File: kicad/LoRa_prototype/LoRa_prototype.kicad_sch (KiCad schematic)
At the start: 6 parts, among them J1 Conn_ST_STDC14, J2 U.FL, U3 AS179-92LF

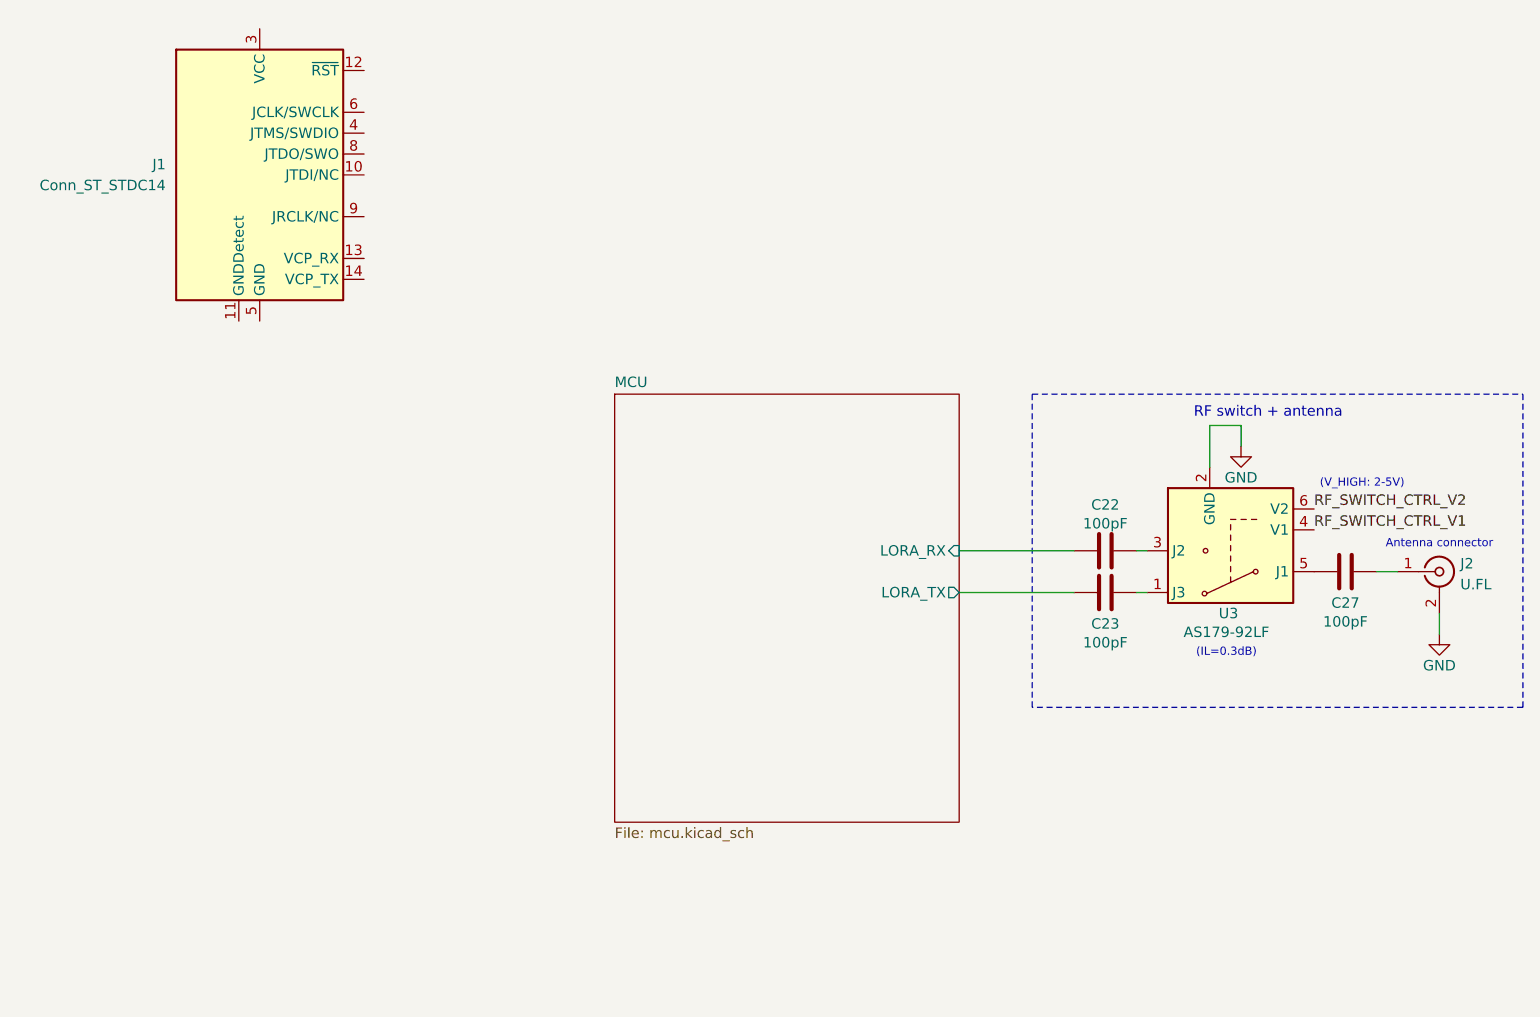
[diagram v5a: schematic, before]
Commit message: Schematic for programming interface done
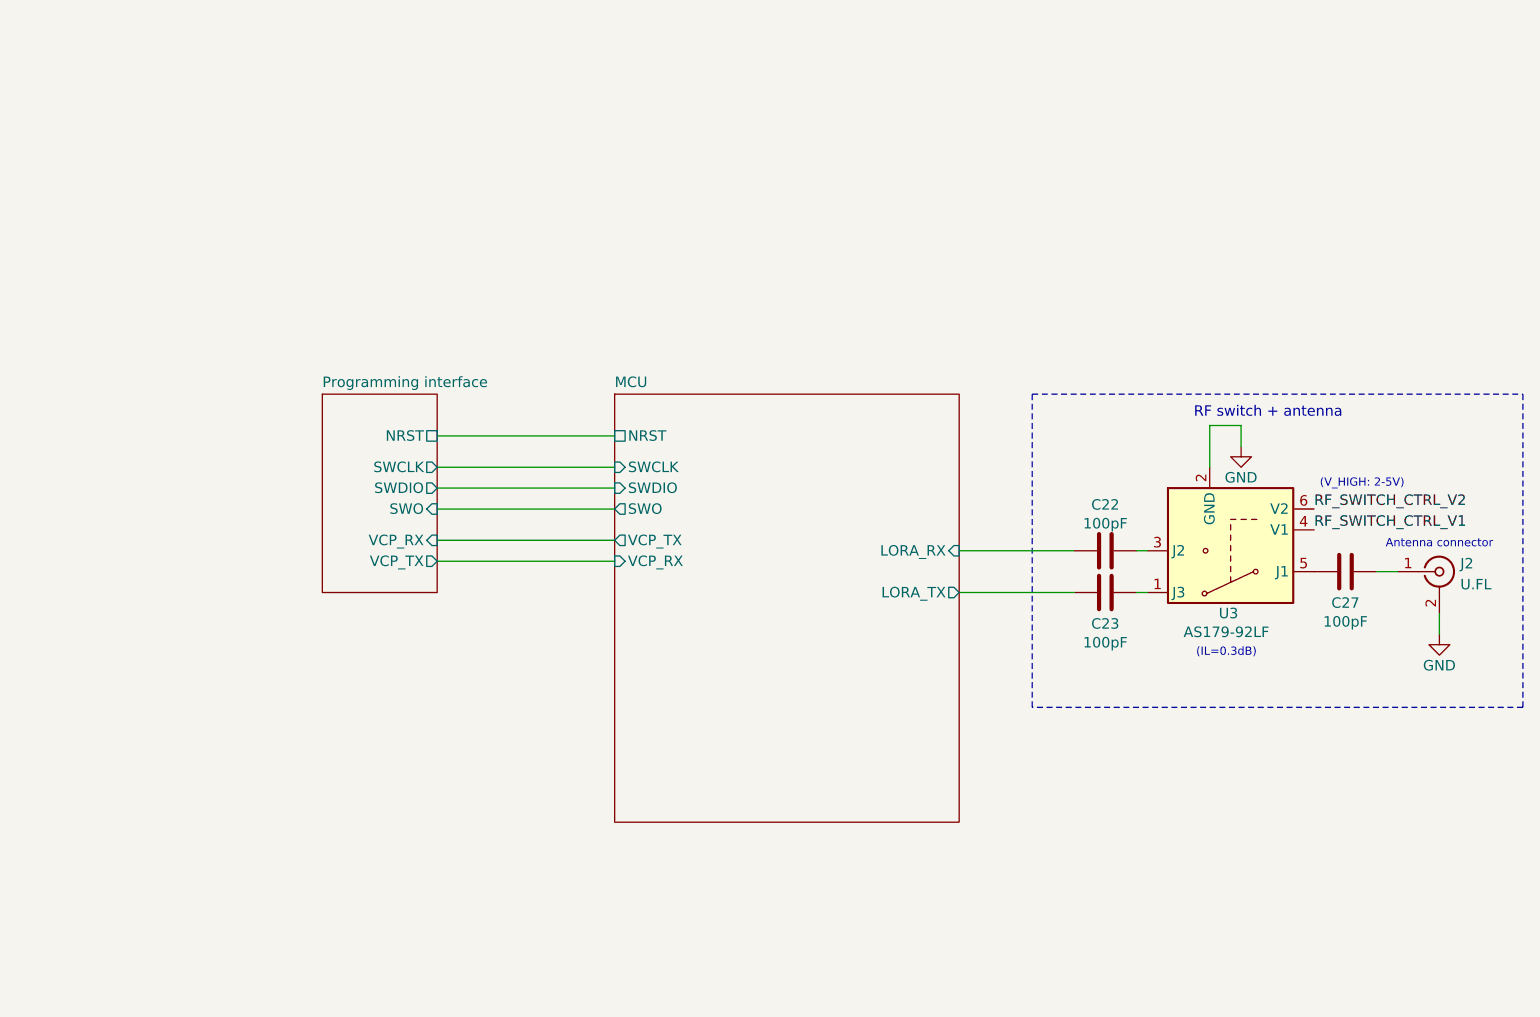
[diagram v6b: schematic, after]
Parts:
- removed J1: Conn_ST_STDC14, Connector_PinHeader_1.27mm:PinHeader_2x07_P1.27mm_Vertical, symbol Connector:Conn_ST_STDC14
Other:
- added sheet Programming interface (programming_interface.kicad_sch)
- sheet MCU ports: added NRST, SWCLK, SWDIO, SWO, VCP_RX, VCP_TX; removed none
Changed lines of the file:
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@@
+	(wire
+		(pts
+			(xy 74.93 96.52) (xy 96.52 96.52)
+		)
+		(stroke
+			(width 0)
+			(type default)
+		)
+	)
 	(wire
 		(pts
@@
 	(wire
 		(pts
+			(xy 74.93 93.98) (xy 96.52 93.98)
+		)
+		(stroke
+			(width 0)
+			(type default)
+		)
+	)
+	(wire
+		(pts
+			(xy 74.93 81.28) (xy 96.52 81.28)
+		)
+		(stroke
+			(width 0)
+			(type default)
+		)
+	)
+	(wire
+		(pts
+			(xy 74.93 90.17) (xy 96.52 90.17)
+		)
+		(stroke
+			(width 0)
+			(type default)
+		)
+	)
+	(wire
+		(pts
 			(xy 172.72 82.55) (xy 172.72 80.01)
 		)
@@
 	(wire
 		(pts
+			(xy 74.93 85.09) (xy 96.52 85.09)
+		)
+		(stroke
+			(width 0)
+			(type default)
+		)
+	)
+	(wire
+		(pts
 			(xy 138.43 100.33) (xy 152.4 100.33)
 		)
@@
 		(pts
 			(xy 138.43 95.25) (xy 152.4 95.25)
+		)
+		(stroke
+			(width 0)
+			(type default)
+		)
+	)
+	(wire
+		(pts
+			(xy 74.93 87.63) (xy 96.52 87.63)
 		)
 		(stroke
@@
 	)
 	(symbol
-		(lib_id "Connector:Conn_ST_STDC14")
-		(at 53.34 49.53 0)
-		(unit 1)
-		(exclude_from_sim no)
-		(in_bom yes)
-		(on_board yes)
-		(dnp no)
-		(fields_autoplaced yes)
-		(property "Reference" "J1"
-			(at 41.91 48.2599 0)
-			(effects
-				(font
-					(size 1.27 1.27)
-				)
-				(justify right)
-			)
-		)
-		(property "Value" "Conn_ST_STDC14"
-			(at 41.91 50.7999 0)
-			(effects
-				(font
-					(size 1.27 1.27)
-				)
-				(justify right)
-			)
-		)
-		(property "Footprint" "Connector_PinHeader_1.27mm:PinHeader_2x07_P1.27mm_Vertical"
-			(at 53.34 49.53 0)
-			(effects
-				(font
-					(size 1.27 1.27)
-				)
-				(hide yes)
-			)
-		)
-		(property "Datasheet" "https://www.st.com/content/ccc/resource/technical/document/user_manual/group1/99/49/91/b6/b2/3a/46/e5/DM00526767/files/DM00526767.pdf/jcr:content/translations/en.DM00526767.pdf"
-			(at 44.45 81.28 90)
-			(effects
-				(font
-					(size 1.27 1.27)
-				)
-				(hide yes)
-			)
-		)
-		(property "Description" "ST Debug Connector, standard ARM Cortex-M SWD and JTAG interface plus UART"
-			(at 53.34 49.53 0)
-			(effects
-				(font
-					(size 1.27 1.27)
-				)
-				(hide yes)
-			)
-		)
-		(pin "1"
-		)
-		(pin "12"
-		)
-		(pin "5"
-		)
-		(pin "6"
-		)
-		(pin "11"
-		)
-		(pin "13"
-		)
-		(pin "10"
-		)
-		(pin "4"
-		)
-		(pin "9"
-		)
-		(pin "8"
-		)
-		(pin "14"
-		)
-		(pin "2"
-		)
-		(pin "7"
-		)
-		(pin "3"
-		)
-		(instances
-			(project ""
-				(path "/9fad4700-f514-47ad-821a-b4076ecc08de"
-					(reference "J1")
-					(unit 1)
-				)
-			)
-		)
-	)
-	(symbol
 		(lib_id "Device:C")
 		(at 156.21 100.33 90)
@@
 	)
 	(sheet
+		(at 60.96 76.2)
+		(size 13.97 24.13)
+		(exclude_from_sim no)
+		(in_bom yes)
+		(on_board yes)
+		(dnp no)
+		(fields_autoplaced yes)
+		(stroke
+			(width 0.1524)
+			(type solid)
+		)
+		(fill
+			(color 0 0 0 0.0000)
+		)
+		(property "Sheetname" "Programming interface"
+			(at 60.96 75.4884 0)
+			(effects
+				(font
+					(size 1.27 1.27)
+				)
+				(justify left bottom)
+			)
+		)
+		(property "Sheetfile" "programming_interface.kicad_sch"
+			(at 60.96 100.9146 0)
+			(effects
+				(font
+					(size 1.27 1.27)
+				)
+				(justify left top)
+				(hide yes)
+			)
+		)
+		(pin "VCP_RX" input
+			(at 74.93 93.98 0)
+			(effects
+				(font
+					(size 1.27 1.27)
+				)
+				(justify right)
+			)
+		)
+		(pin "SWO" input
+			(at 74.93 90.17 0)
+			(effects
+				(font
+					(size 1.27 1.27)
+				)
+				(justify right)
+			)
+		)
+		(pin "VCP_TX" output
+			(at 74.93 96.52 0)
+			(effects
+				(font
+					(size 1.27 1.27)
+				)
+				(justify right)
+			)
+		)
+		(pin "SWDIO" output
+			(at 74.93 87.63 0)
+			(effects
+				(font
+					(size 1.27 1.27)
+				)
+				(justify right)
+			)
+		)
+		(pin "SWCLK" output
+			(at 74.93 85.09 0)
+			(effects
+				(font
+					(size 1.27 1.27)
+				)
+				(justify right)
+			)
+		)
+		(pin "NRST" passive
+			(at 74.93 81.28 0)
+			(effects
+				(font
+					(size 1.27 1.27)
+				)
+				(justify right)
+			)
+		)
+		(instances
+			(project "LoRa_prototype"
+				(path "/9fad4700-f514-47ad-821a-b4076ecc08de"
+					(page "3")
+				)
+			)
+		)
+	)
+	(sheet
 		(at 96.52 76.2)
 		(size 41.91 52.07)
@@
 				)
 				(justify left top)
+				(hide yes)
 			)
 		)
@@
 			)
 		)
+		(pin "NRST" passive
+			(at 96.52 81.28 180)
+			(effects
+				(font
+					(size 1.27 1.27)
+				)
+				(justify left)
+			)
+		)
+		(pin "SWDIO" input
+			(at 96.52 87.63 180)
+			(effects
+				(font
+					(size 1.27 1.27)
+				)
+				(justify left)
+			)
+		)
+		(pin "SWCLK" input
+			(at 96.52 85.09 180)
+			(effects
+				(font
+					(size 1.27 1.27)
+				)
+				(justify left)
+			)
+		)
+		(pin "SWO" output
+			(at 96.52 90.17 180)
+			(effects
+				(font
+					(size 1.27 1.27)
+				)
+				(justify left)
+			)
+		)
+		(pin "VCP_TX" output
+			(at 96.52 93.98 180)
+			(effects
+				(font
+					(size 1.27 1.27)
+				)
+				(justify left)
+			)
+		)
+		(pin "VCP_RX" input
+			(at 96.52 96.52 180)
+			(effects
+				(font
+					(size 1.27 1.27)
+				)
+				(justify left)
+			)
+		)

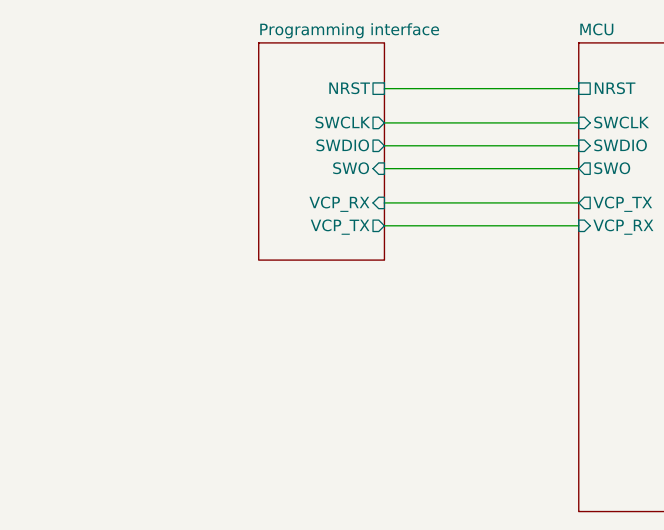
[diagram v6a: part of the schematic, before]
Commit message: Add SPV1050 symbol in schematic
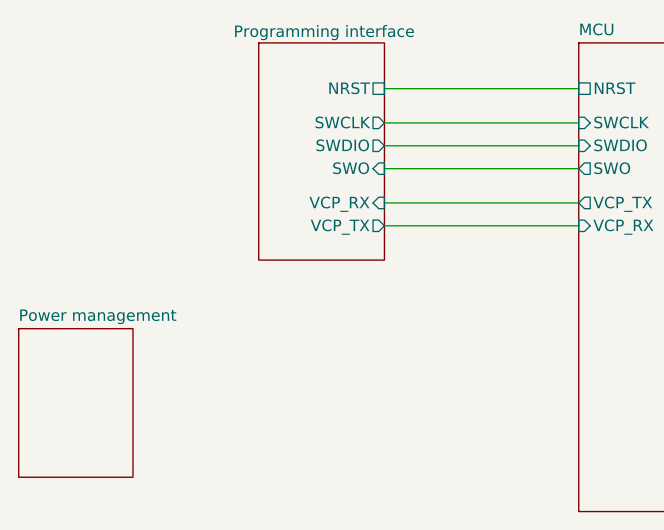
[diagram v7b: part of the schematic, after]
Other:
- added sheet Power management (power.kicad_sch)
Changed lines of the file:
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@@
 	)
 	(sheet
-		(at 60.96 76.2)
-		(size 13.97 24.13)
+		(at 34.29 107.95)
+		(size 12.7 16.51)
 		(exclude_from_sim no)
 		(in_bom yes)
@@
 			(color 0 0 0 0.0000)
 		)
-		(property "Sheetname" "Programming interface"
-			(at 60.96 75.4884 0)
+		(property "Sheetname" "Power management"
+			(at 34.29 107.2384 0)
 			(effects
 				(font
+					(size 1.27 1.27)
+				)
+				(justify left bottom)
+			)
+		)
+		(property "Sheetfile" "power.kicad_sch"
+			(at 34.29 125.0446 0)
+			(effects
+				(font
+					(size 1.27 1.27)
+				)
+				(justify left top)
+				(hide yes)
+			)
+		)
+		(instances
+			(project "LoRa_prototype"
+				(path "/9fad4700-f514-47ad-821a-b4076ecc08de"
+					(page "4")
+				)
+			)
+		)
+	)
+	(sheet
+		(at 60.96 76.2)
+		(size 13.97 24.13)
+		(exclude_from_sim no)
+		(in_bom yes)
+		(on_board yes)
+		(dnp no)
+		(stroke
+			(width 0.1524)
+			(type solid)
+		)
+		(fill
+			(color 0 0 0 0.0000)
+		)
+		(property "Sheetname" "Programming interface"
+			(at 58.166 75.692 0)
+			(effects
+				(font
